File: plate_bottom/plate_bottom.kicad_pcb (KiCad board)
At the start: 2 copper layers, 178.4 x 118.1 mm, 15 parts

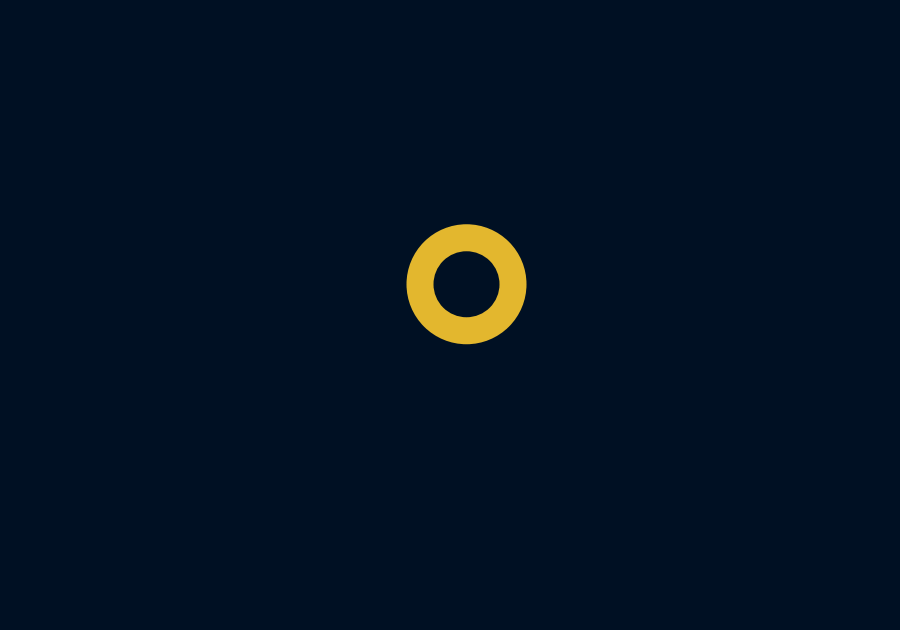
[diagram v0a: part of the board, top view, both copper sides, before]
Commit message: - Added encoders to their place. Not routed yet. - Moved one case hole. Both on pcb and bottom-plate.
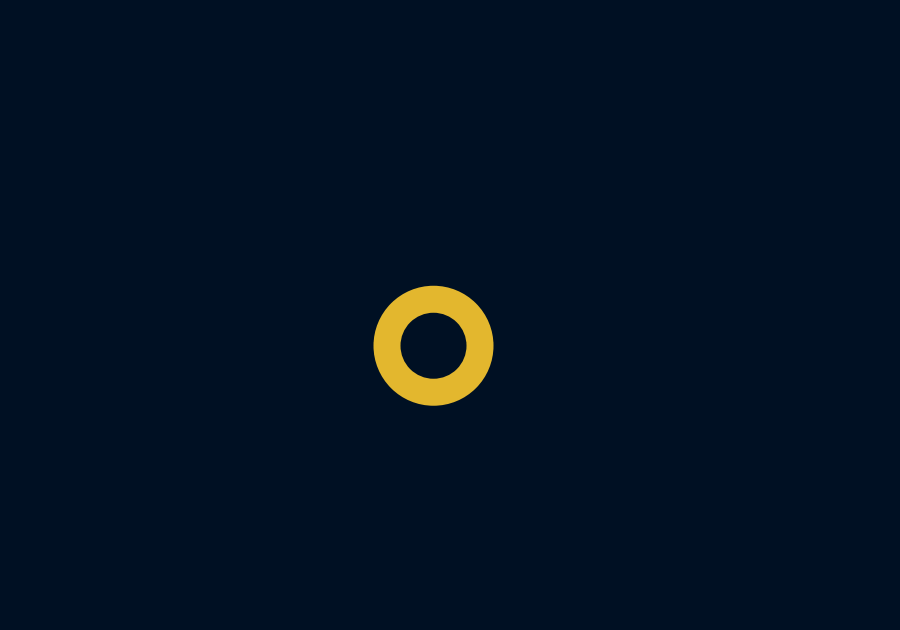
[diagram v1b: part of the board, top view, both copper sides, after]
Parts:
- moved HM1 2.33 mm to (215.6, 122.9)
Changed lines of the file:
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@@
+  )
+  (module used_footprints:M2_HOLE_PCB (layer F.Cu)
+    (at 215.55 122.9)
+    (fp_text reference HM1 (at 0 2.7) (layer F.SilkS) hide
+      (effects (font (size 1 1) (thickness 0.15)))
+    )
+    (fp_text value CaseHole (at 0 -2.6) (layer F.Fab) hide
+      (effects (font (size 1 1) (thickness 0.15)))
+    )
+    (pad "" thru_hole circle (at 0 0) (size 4 4) (drill 2.2) (layers *.Cu *.Mask))
   )
   (module used_footprints:M2_HOLE_PCB (layer F.Cu)
@@
       (effects (font (size 1 1) (thickness 0.15)))
     )
-    (fp_text value CaseHole (at 0 -2.6) (layer F.Fab) hide
-      (effects (font (size 1 1) (thickness 0.15)))
-    )
-    (pad "" thru_hole circle (at 0 0) (size 4 4) (drill 2.2) (layers *.Cu *.Mask))
-  )
-  (module used_footprints:M2_HOLE_PCB (layer F.Cu)
-    (at 216.65 120.85)
-    (fp_text reference HM1 (at 0 2.7) (layer F.SilkS) hide
-      (effects (font (size 1 1) (thickness 0.15)))
-    )

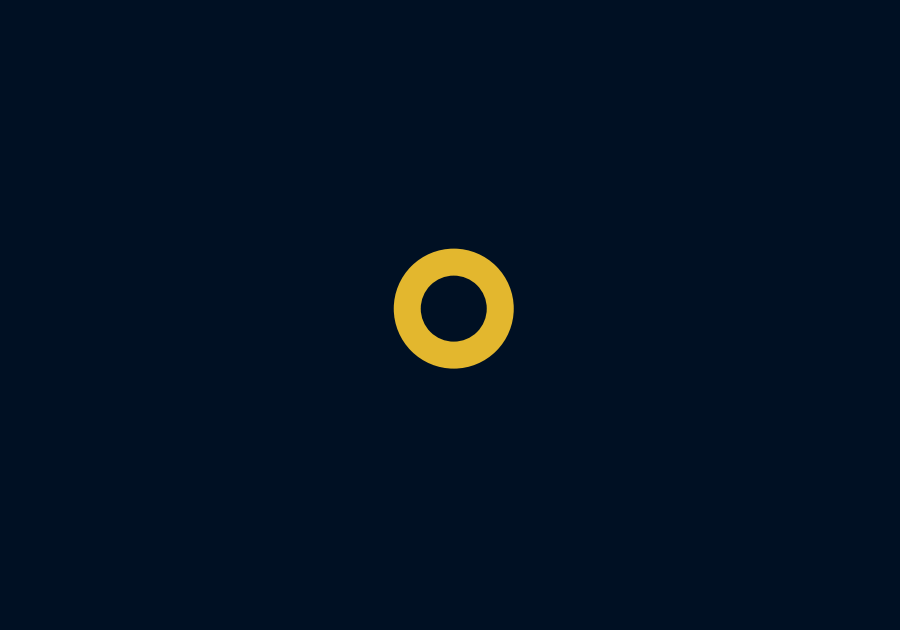
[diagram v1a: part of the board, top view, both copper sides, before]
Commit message: Moved case hole more downwards
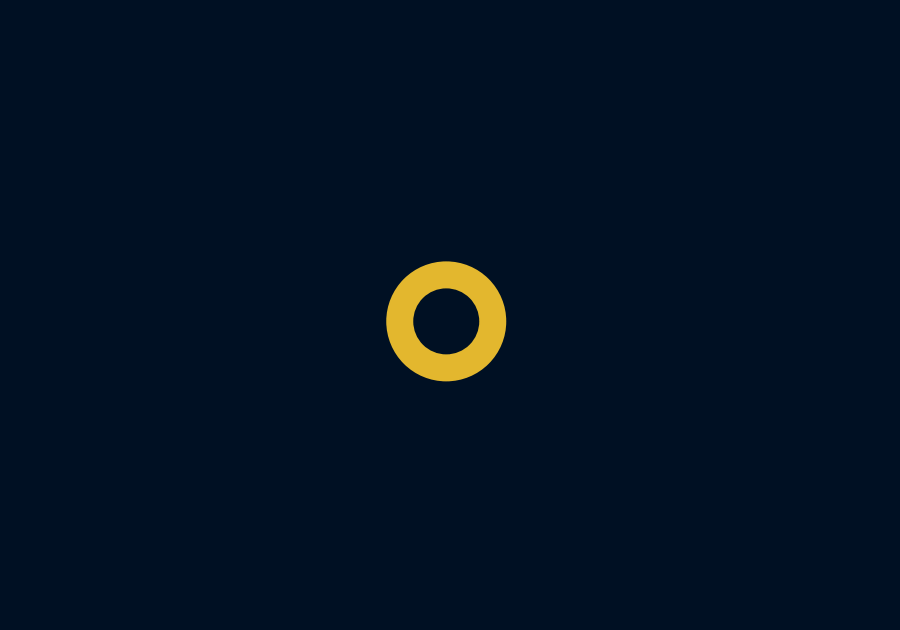
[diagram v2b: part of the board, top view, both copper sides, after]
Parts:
- moved HM1 0.49 mm to (215.3, 123.3)
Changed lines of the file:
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@@
   )
   (module used_footprints:M2_HOLE_PCB (layer F.Cu)
-    (at 215.55 122.9)
+    (at 215.3 123.325)
     (fp_text reference HM1 (at 0 2.7) (layer F.SilkS) hide
       (effects (font (size 1 1) (thickness 0.15)))

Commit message: WIP on diodes. Moved a case hole a little bit
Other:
- outline, holes or cut-outs redrawn
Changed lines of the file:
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@@
       (effects (font (size 1 1) (thickness 0.15)))
     )
-    (pad "" np_thru_hole circle (at 0 0) (size 2.2 2.2) (drill 2.2) (layers *.Cu *.Mask))
+    (pad "" np_thru_hole circle (at 0 0.55) (size 2.2 2.2) (drill 2.2) (layers *.Cu *.Mask))
   )
   (gr_line (start 254.95 99.8) (end 254.95 95.65) (layer Dwgs.User) (width 0.15))
@@
   (gr_line (start 76.55 99.84) (end 76.55 83.01) (layer Edge.Cuts) (width 0.05))
   (gr_arc (start 95.099999 86.99) (end 95.599997 86.99) (angle -180) (layer Edge.Cuts) (width 0.05))
-  (gr_line (start 94.600001 92.589999) (end 94.600001 86.99) (layer Edge.Cuts) (width 0.05))
-  (gr_line (start 95.6 86.99) (end 95.599999 92.590001) (layer Edge.Cuts) (width 0.05))
-  (gr_arc (start 95.1 92.59) (end 94.600001 92.589999) (angle -180) (layer Edge.Cuts) (width 0.05))
+  (gr_line (start 94.600001 93.449999) (end 94.600001 86.99) (layer Edge.Cuts) (width 0.05))
+  (gr_line (start 95.6 86.99) (end 95.599999 93.450001) (layer Edge.Cuts) (width 0.05))
+  (gr_arc (start 95.1 93.45) (end 94.600001 93.449999) (angle -180) (layer Edge.Cuts) (width 0.05))
   (gr_arc (start 95.1 84) (end 94.600001 84) (angle -180) (layer Edge.Cuts) (width 0.05))
   (gr_arc (start 93.6 99.84) (end 93.6 100.84) (angle -90) (layer Edge.Cuts) (width 0.05))

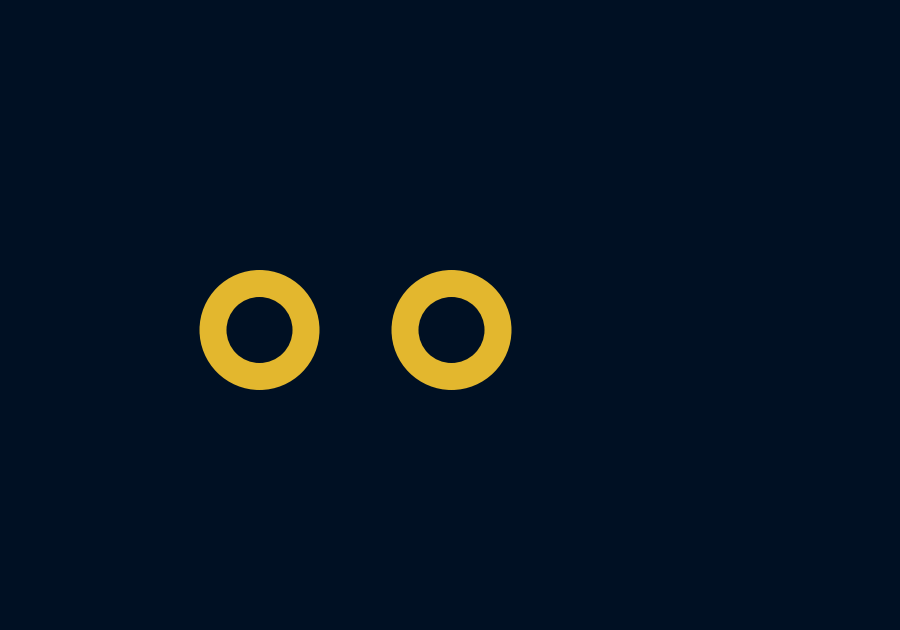
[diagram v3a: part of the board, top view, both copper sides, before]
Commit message: Routing encoder after rotate. Moved case hole a little.
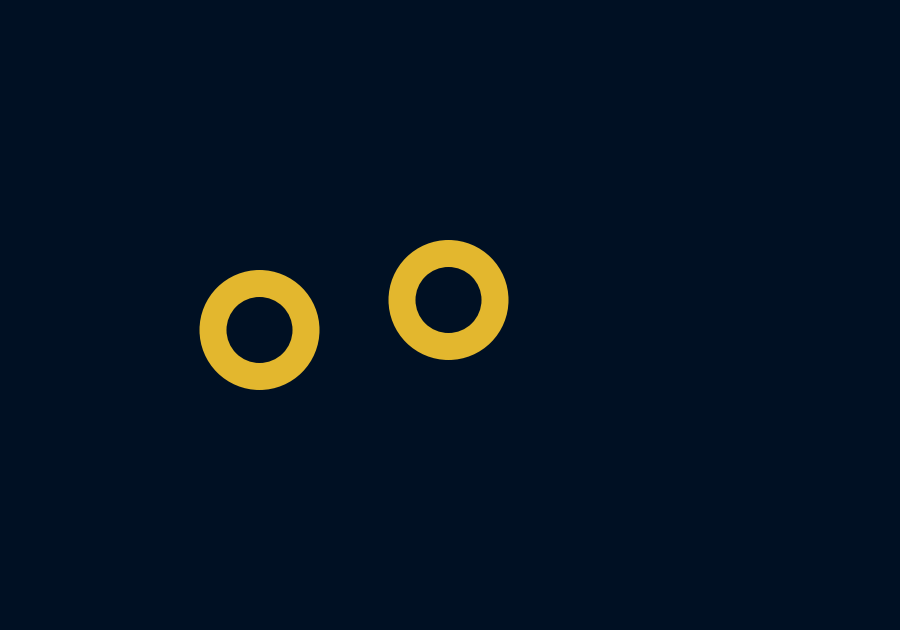
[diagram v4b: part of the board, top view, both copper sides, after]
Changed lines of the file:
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@@
     (mod_text_size 1 1)
     (mod_text_width 0.15)
-    (pad_size 2.2 2.2)
+    (pad_size 4 4)
     (pad_drill 2.2)
     (pad_to_mask_clearance 0)
@@
       (effects (font (size 1 1) (thickness 0.15)))
     )
-    (pad "" thru_hole circle (at 0 0) (size 4 4) (drill 2.2) (layers *.Cu *.Mask))
+    (pad "" thru_hole circle (at -0.1 -1) (size 4 4) (drill 2.2) (layers *.Cu *.Mask))
   )
   (module used_footprints:M2_HOLE_PCB (layer F.Cu)

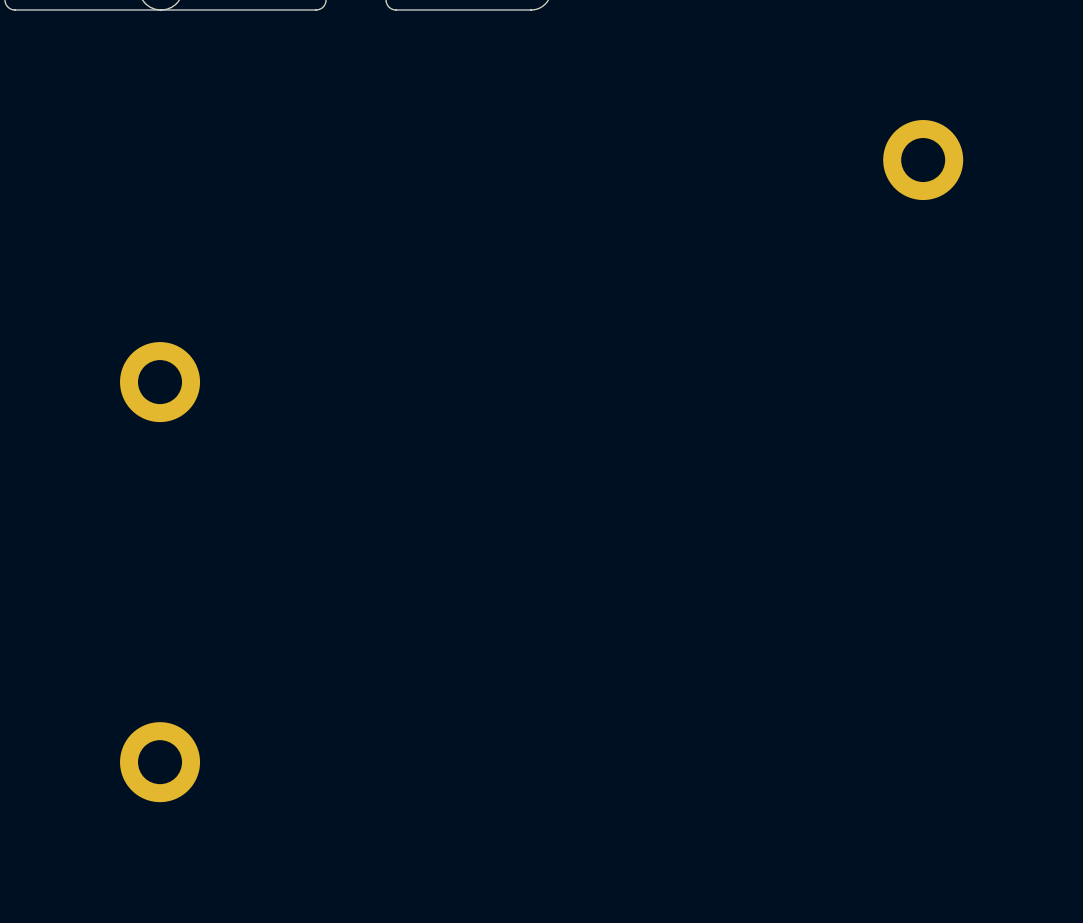
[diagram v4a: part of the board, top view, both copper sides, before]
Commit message: Replaced diode footprints with smd+th
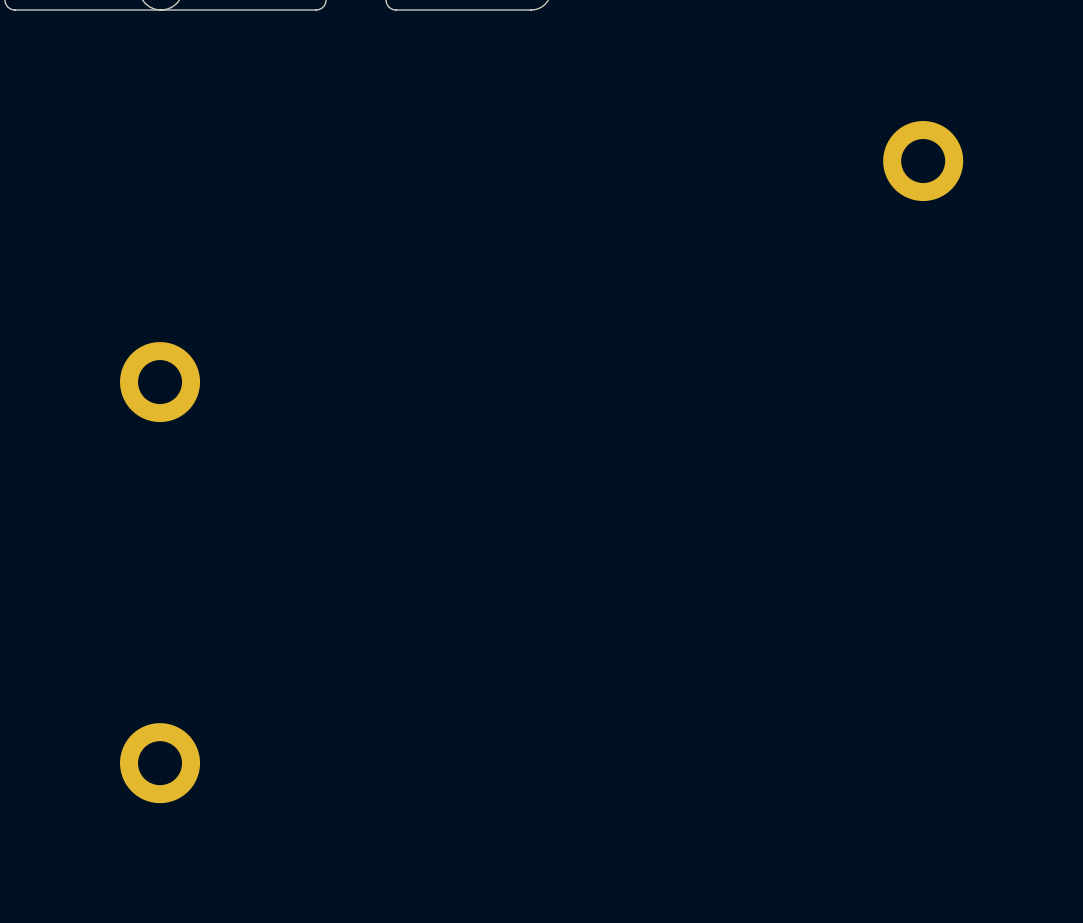
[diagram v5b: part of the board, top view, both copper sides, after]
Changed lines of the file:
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@@
       (effects (font (size 1 1) (thickness 0.15)))
     )
-    (pad "" thru_hole circle (at 0 0) (size 4 4) (drill 2.2) (layers *.Cu *.Mask))
+    (pad "" thru_hole circle (at 0 0.05) (size 4 4) (drill 2.2) (layers *.Cu *.Mask))
   )
   (module used_footprints:M2_HOLE_PCB (layer F.Cu)
@@
       (effects (font (size 1 1) (thickness 0.15)))
     )
-    (pad "" thru_hole circle (at 0 0) (size 4 4) (drill 2.2) (layers *.Cu *.Mask))
+    (pad "" thru_hole circle (at 0 0.05) (size 4 4) (drill 2.2) (layers *.Cu *.Mask))
   )
   (module used_footprints:M2_HOLE_PCB (layer F.Cu)
